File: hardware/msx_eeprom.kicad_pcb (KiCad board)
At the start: 2 copper layers, 102.8 x 65.4 mm, 101 parts, among them J1 Conn_02x07_Odd_Even, P1 MSX_CONNECTOR, U1 AT28C256-15PU

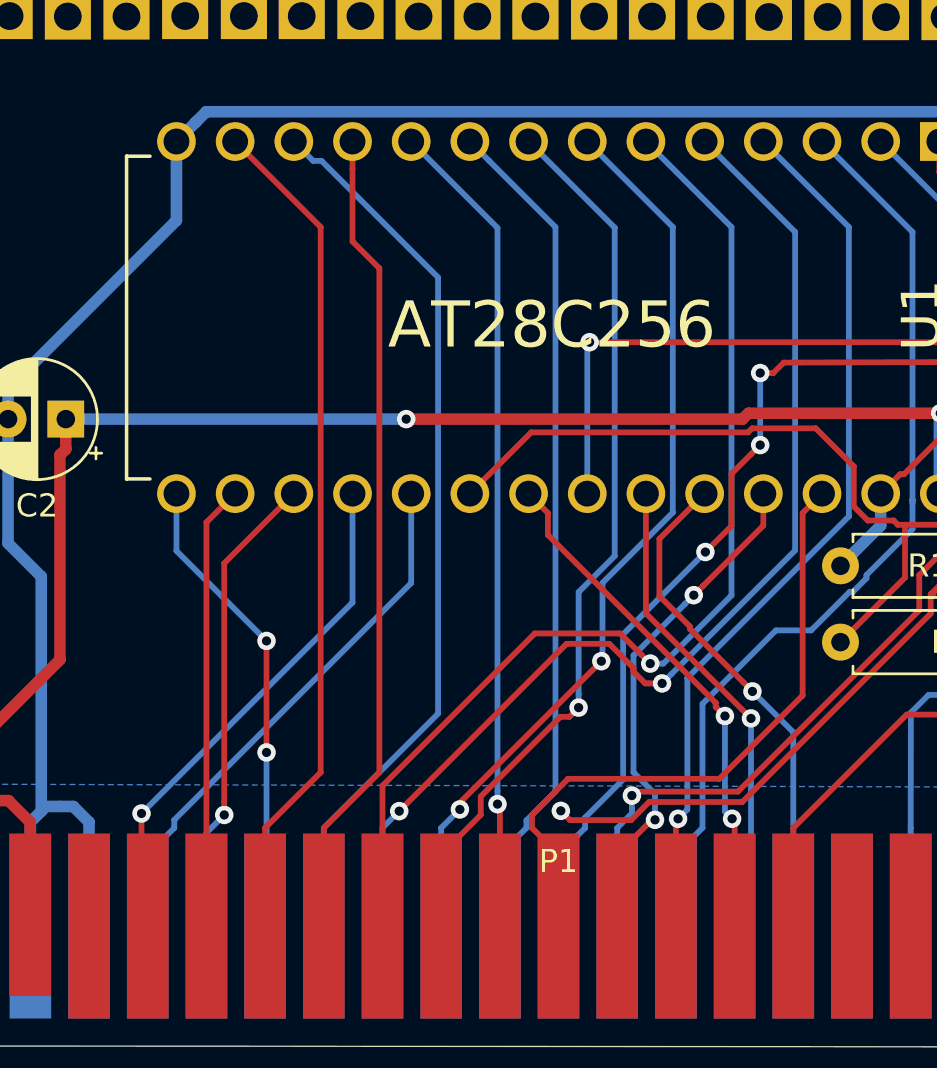
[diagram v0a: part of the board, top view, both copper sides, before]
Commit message: Update schema to Rev.3. Added pull up resistor to /MEM_CE
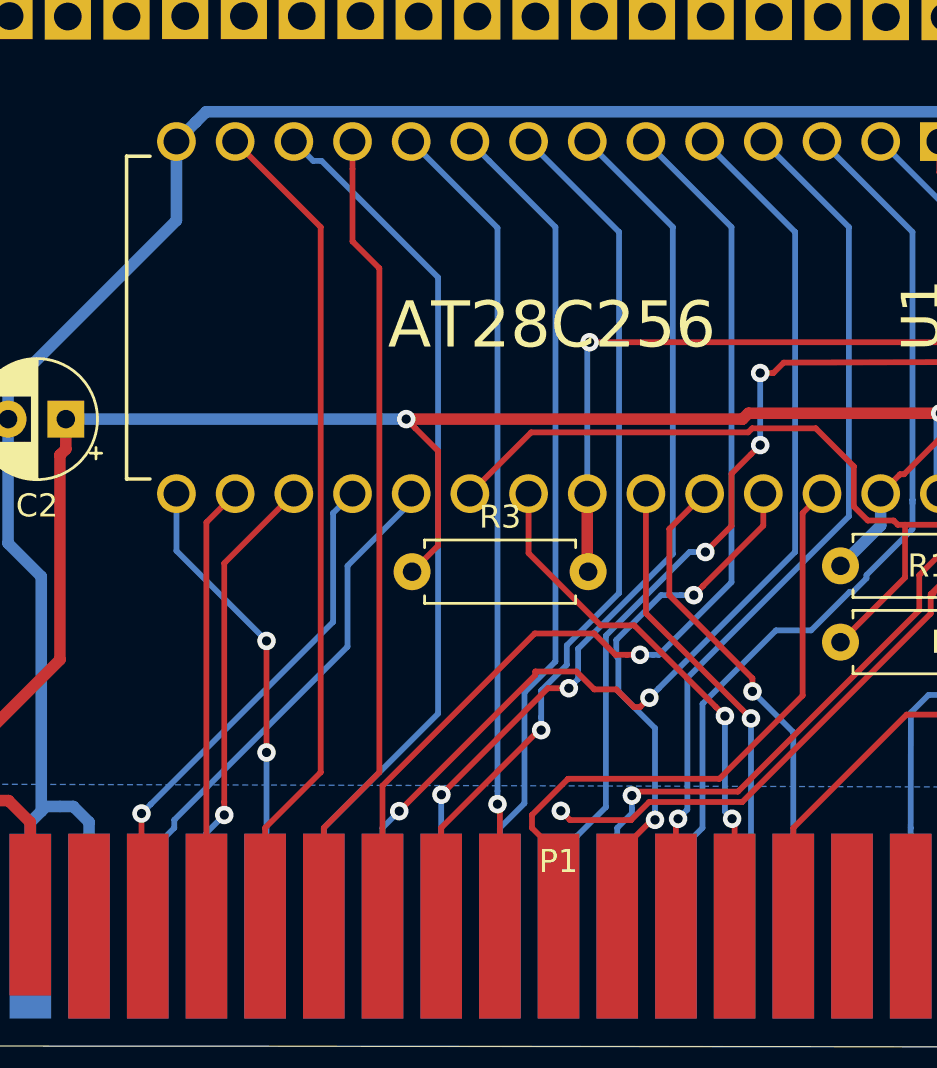
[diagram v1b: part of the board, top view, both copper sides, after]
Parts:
- added R3: 10K, Resistor_THT:R_Axial_DIN0207_L6.3mm_D2.5mm_P7.62mm_Horizontal, F.Cu at (132.1, 74.2)
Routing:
- net +5V: track 83.6 -> 91.2 mm
- net mem_oe: track 46.4 -> 49.8 mm
- net A8: track 22.2 -> 23.6 mm
- net A10: track 22.4 -> 23.3 mm
- net A4: track 46.9 -> 46.2 mm
- net A3: track 39.6 -> 40.2 mm
